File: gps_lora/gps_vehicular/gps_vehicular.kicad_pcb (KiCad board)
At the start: 2 copper layers, 71.1 x 41.3 mm, 53 parts, among them J1 IN 12V, J2 USB_B, J3 ADJ, J4 BAT, J5 IGN, J6 RELAY, J7 PANI, J8 SWD, Q1 Q_PMOS_GSD, Q2 SMMBT3904LT1G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

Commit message: add pcb gps vehicular and minimo
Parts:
- AE1, D9, Q3, R10, R11, R12, R13, R14, R15, U4, U5, U7: moved to F.Cu
- C7, D5, D6, D7, J1, J2, J3, J4, J5, J6, J7, J8, MODULE1, R3, R6, R8, SW1: moved to B.Cu
- moved D5 25.6 mm to (118.4, 55.9)
- moved R11 24.8 mm to (133.9, 78.7)
- moved U7 23.7 mm to (163.3, 82.5), turned to 180 degrees
- moved D9 23.3 mm to (163.8, 86.9)
- moved R3 22.6 mm to (118.4, 61.7)
- moved R15 21.3 mm to (162.1, 79.0)
- moved R13 19.7 mm to (143.0, 82.3), turned to 90 degrees
- moved R14 18.8 mm to (169.4, 82.3), turned to 90 degrees
- moved U4 18.6 mm to (135.1, 82.5), turned to 180 degrees
- moved R10 18.4 mm to (140.2, 87.4)
- moved D7 15.9 mm to (123.2, 56.0), turned to 90 degrees
- moved C5 15.3 mm to (114.8, 82.3), turned to 180 degrees
- moved R9 15.2 mm to (123.7, 82.0), turned to 90 degrees
- moved Q3 14.9 mm to (151.6, 86.7), turned to 0 degrees
- moved C1 14.5 mm to (114.8, 66.8), turned to 180 degrees
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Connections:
- U6 pad 1: Net-(U6-Pad1) -> /microcontroller/LED_1
- U6 pad 12: Net-(U6-Pad12) -> /microcontroller/SIG_PANI
- U6 pad 15: Net-(U6-Pad15) -> /microcontroller/1PPS
- U6 pad 2: Net-(U6-Pad2) -> /microcontroller/LED_2
- U6 pad 6: Net-(U6-Pad6) -> /microcontroller/SIG_CONECTADO
- U6 pad 7: Net-(U6-Pad7) -> /microcontroller/SIG_IGNI
- U6 pad 8: Net-(U6-Pad8) -> /microcontroller/OUT_SIG
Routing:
- net +3V3: track 0.00 -> 200.1 mm, vias 0 -> 4
- net +5V: track 0.00 -> 63.7 mm, vias 0 -> 2
- net +12V: track 0.00 -> 58.5 mm
- net D+: track 0.00 -> 37.8 mm, vias 0 -> 1
- net D-: track 0.00 -> 37.8 mm, vias 0 -> 1
- net +BATT: track 0.00 -> 37.8 mm
- net Net-(R3-Pad2): track 0.00 -> 36.7 mm, vias 0 -> 3
- net /microcontroller/SIG_PANI: track 0.00 -> 35.6 mm
- net /microcontroller/SIG_CONECTADO: track 0.00 -> 30.8 mm, vias 0 -> 1
- net /microcontroller/DIO0: track 0.00 -> 29.3 mm, vias 0 -> 2
- net GND: track 0.00 -> 27.8 mm, vias 0 -> 9
- net /microcontroller/DIO1: track 0.00 -> 24.6 mm, vias 0 -> 2
- net /microcontroller/DIO2: track 0.00 -> 22.7 mm
- net /microcontroller/RX_GPS: track 0.00 -> 22.5 mm, vias 0 -> 1
- net /microcontroller/LED_2: track 0.00 -> 21.2 mm, vias 0 -> 1
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- added copper zone on B.Cu, net GND
- added copper zone on F.Cu, net GND
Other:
- board size 71.1 x 41.3 mm -> 71.1 x 42.8 mm
- net class Default: trace_width 0.25 -> 0.3; via_drill 0.4 -> 0.3
- net class Source added: clearance 0.2, trace_width 0.5, via_dia 0.9, via_drill 0.45
- board text added: "+"
- board text added: "-"
- board text added: "1"

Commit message: add logos
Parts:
- added G***: LOGO, Aesthetics:electronic_cats_logo_8x6, B.Cu at (158.6, 56.8)
- added REF***: OSHW-Logo_7.5x8mm_SilkScreen, Symbols:OSHW-Logo_7.5x8mm_SilkScreen, F.Cu at (122.8, 56.1)
- added REF***: FCC-Logo_7.3x6mm_SilkScreen, Symbols:FCC-Logo_7.3x6mm_SilkScreen, F.Cu at (108.1, 86.4)

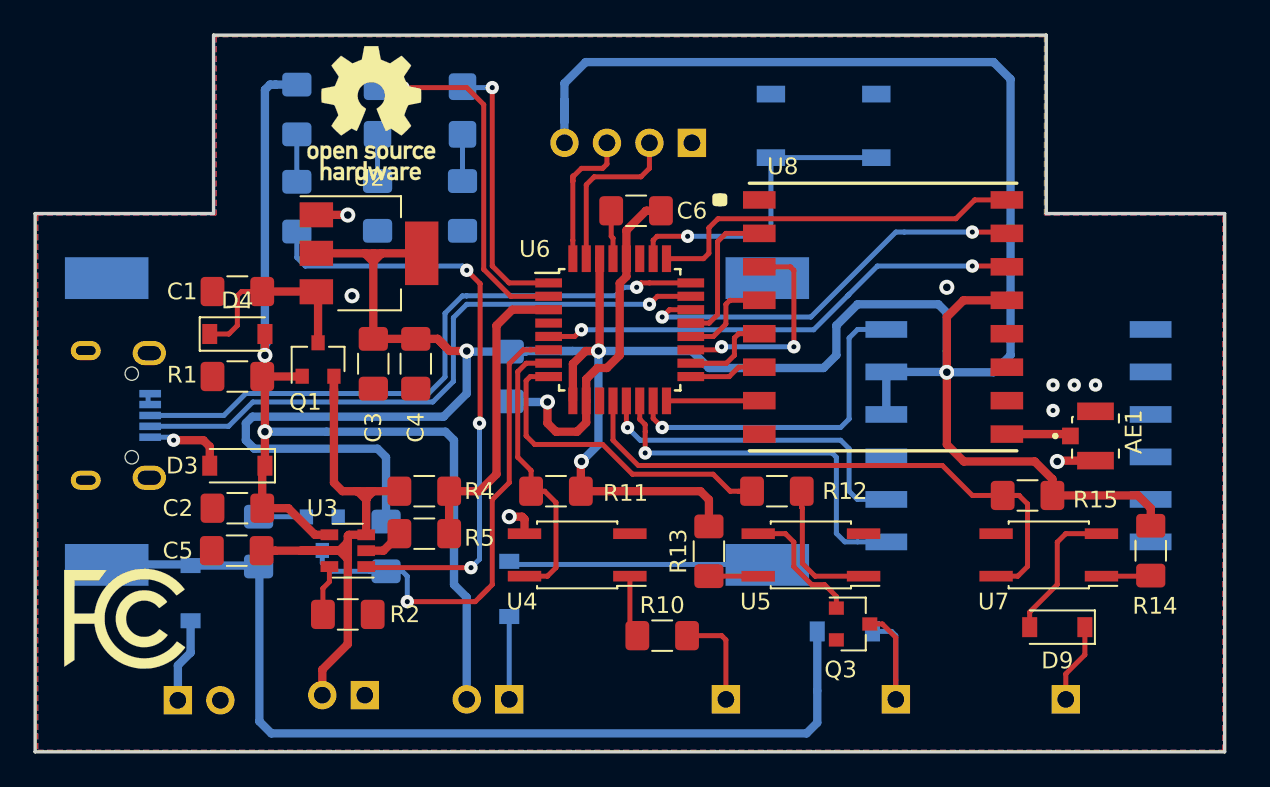
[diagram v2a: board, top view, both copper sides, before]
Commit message: Round off the corners and change screen printing gps_vehicular
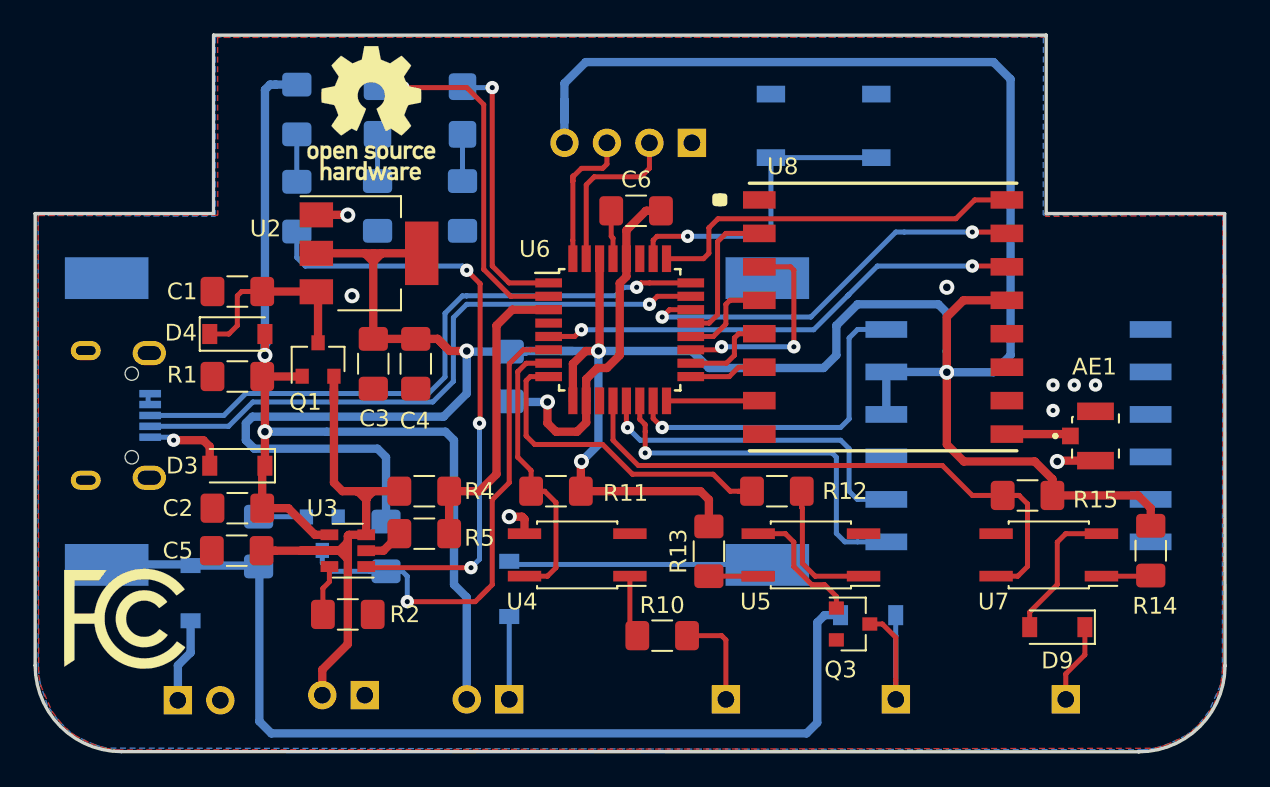
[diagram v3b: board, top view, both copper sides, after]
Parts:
- moved D8 1.70 mm to (152.5, 86.2)
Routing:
- net +12V: track 58.5 -> 60.6 mm
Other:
- outline, holes or cut-outs redrawn
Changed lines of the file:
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@@
-(kicad_pcb (version 20171130) (host pcbnew "(5.0.1-3-g963ef8bb5)")
+(kicad_pcb (version 20171130) (host pcbnew "(5.1.0)-1")
   (general
     (thickness 1.6)
-    (drawings 14)
-    (tracks 470)
+    (drawings 16)
+    (tracks 471)
     (zones 0)
     (modules 56)
@@
     (zone_45_only no)
     (trace_min 0.2)
-    (segment_width 0.2)
-    (edge_width 0.15)
     (via_size 0.8)
     (via_drill 0.3)
@@
     (uvia_min_size 0.2)
     (uvia_min_drill 0.1)
+    (edge_width 0.15)
+    (segment_width 0.2)
     (pcb_text_width 0.3)
     (pcb_text_size 1.5 1.5)
@@
     (at 166.116 75.438 270)
     (attr smd)
-    (fp_text reference AE1 (at -0.254 -2.286 90) (layer F.SilkS)
+    (fp_text reference AE1 (at -4.138 0.066 180) (layer F.SilkS)
       (effects (font (size 1 1) (thickness 0.15)))
     )
@@
     (tags "capacitor handsolder")
     (attr smd)
-    (fp_text reference C3 (at 3.81 0 270) (layer F.SilkS)
+    (fp_text reference C3 (at 3.27 -0.064) (layer F.SilkS)
       (effects (font (size 1 1) (thickness 0.15)))
     )
@@
     (tags "capacitor handsolder")
     (attr smd)
-    (fp_text reference C4 (at 3.81 0 270) (layer F.SilkS)
+    (fp_text reference C4 (at 3.41 0.046) (layer F.SilkS)
       (effects (font (size 1 1) (thickness 0.15)))
     )
@@
     (tags "capacitor handsolder")
     (attr smd)
-    (fp_text reference C6 (at 3.3385 0) (layer F.SilkS)
+    (fp_text reference C6 (at 0.0125 -1.866) (layer F.SilkS)
       (effects (font (size 1 1) (thickness 0.15)))
     )
@@
     (tags "capacitor handsolder")
     (attr smd)
-    (fp_text reference C7 (at 0 1.82 270) (layer B.SilkS)
+    (fp_text reference C7 (at -3.252 -0.106) (layer B.SilkS)
       (effects (font (size 1 1) (thickness 0.15)) (justify mirror))
     )
@@
     (tags SOD-123)
     (attr smd)
-    (fp_text reference D1 (at -3.302 0 90) (layer B.SilkS)
+    (fp_text reference D1 (at -3.302 0 180) (layer B.SilkS)
       (effects (font (size 1 1) (thickness 0.15)) (justify mirror))
     )
@@
     (tags SOD-123)
     (attr smd)
-    (fp_text reference D2 (at 3.556 0 90) (layer B.SilkS)
+    (fp_text reference D2 (at 3.556 0 180) (layer B.SilkS)
       (effects (font (size 1 1) (thickness 0.15)) (justify mirror))
     )
@@
   )
   (module Diode_SMD:D_SOD-123 (layer B.Cu)
-    (at 151.13 87.122)
+    (at 152.52 86.15)
     (descr SOD-123)
     (tags SOD-123)
@@
       (effects (font (size 1 1) (thickness 0.05)))
     )
-    (fp_text value L80-M39 (at 5.3 -7.55 180) (layer B.SilkS)
+    (fp_text value L80-M39 (at -5.12 9.04 180) (layer B.SilkS)
       (effects (font (size 1 1) (thickness 0.15)) (justify mirror))
     )
@@
     (tags SOT-23)
     (attr smd)
-    (fp_text reference Q2 (at 2.794 0 90) (layer B.SilkS)
+    (fp_text reference Q2 (at -2.58 -0.052 180) (layer B.SilkS)
       (effects (font (size 1 1) (thickness 0.15)) (justify mirror))
     )
@@
     (tags "resistor handsolder")
     (attr smd)
-    (fp_text reference R7 (at 3.5925 0 90) (layer B.SilkS)
+    (fp_text reference R7 (at -3.4215 0.028 180) (layer B.SilkS)
       (effects (font (size 1 1) (thickness 0.15)) (justify mirror))
     )
@@
     (tags "resistor handsolder")
     (attr smd)
-    (fp_text reference R9 (at -3.556 0 90) (layer B.SilkS)
+    (fp_text reference R9 (at 3.212 0.012 180) (layer B.SilkS)
       (effects (font (size 1 1) (thickness 0.15)) (justify mirror))
     )
@@
     (tags "CMS SOT")
     (attr smd)
-    (fp_text reference U2 (at 0 -4.5) (layer F.SilkS)
+    (fp_text reference U2 (at -6.192 -1.476) (layer F.SilkS)
       (effects (font (size 1 1) (thickness 0.15)))
     )
@@
   (module gps_LoRa:LM2596DC-DC (layer B.Cu)
     (at 105.156 85.09)
-    (fp_text reference U1 (at 4.365 -0.9135) (layer B.SilkS)
+    (fp_text reference U1 (at 2.054 0.9) (layer B.SilkS)
       (effects (font (size 1 1) (thickness 0.15)) (justify mirror))
     )
@@
     (tags SOD-123)
     (attr smd)
-    (fp_text reference D4 (at 0 -2) (layer F.SilkS)
+    (fp_text reference D4 (at -3.378 -0.072) (layer F.SilkS)
       (effects (font (size 1 1) (thickness 0.15)))
     )
@@
       (xy 1.372452 -1.683595)) (layer F.SilkS) (width 0.01))
   )
+  (gr_arc (start 168.71 89.17) (end 168.71 94.32) (angle -90) (layer Edge.Cuts) (width 0.2))
+  (gr_arc (start 107.87 89.16) (end 102.72 89.16) (angle -90) (layer Edge.Cuts) (width 0.2))
   (dimension 16.256 (width 0.15) (layer Margin)
     (gr_text "16.256 mm" (at 100.046 86.106 90) (layer Margin)
@@
   )
   (gr_line (start 113.386 51.472) (end 113.386 62.14) (layer Edge.Cuts) (width 0.2))
-  (gr_line (start 102.718 62.14) (end 102.718 94.3218) (layer Edge.Cuts) (width 0.2))
-  (gr_line (start 173.838 94.3218) (end 173.838 62.14) (layer Edge.Cuts) (width 0.2))
+  (gr_line (start 102.718 62.14) (end 102.72 89.16) (layer Edge.Cuts) (width 0.2))
+  (gr_line (start 173.86 89.17) (end 173.838 62.14) (layer Edge.Cuts) (width 0.2))
   (gr_line (start 173.838 62.14) (end 163.17 62.14) (layer Edge.Cuts) (width 0.2))
   (gr_line (start 163.17 51.472) (end 113.386 51.472) (layer Edge.Cuts) (width 0.2))
-  (gr_line (start 102.718 94.3218) (end 173.838 94.3218) (layer Edge.Cuts) (width 0.2))
+  (gr_line (start 107.87 94.31) (end 168.71 94.32) (layer Edge.Cuts) (width 0.2))
   (gr_line (start 113.386 62.14) (end 102.718 62.14) (layer Edge.Cuts) (width 0.2))
   (gr_line (start 163.17 62.14) (end 163.17 51.472) (layer Edge.Cuts) (width 0.2))
@@
   (segment (start 116.025 83.186) (end 116.078 83.239) (width 0.5) (layer B.Cu) (net 8))
   (segment (start 112.014 83.186) (end 116.025 83.186) (width 0.5) (layer B.Cu) (net 8))
-  (segment (start 116.078 83.239) (end 116.12379 83.28479) (width 0.5) (layer B.Cu) (net 8))
-  (segment (start 149.48 90.678) (end 149.48 87.122) (width 0.5) (layer B.Cu) (net 8))
-  (segment (start 116.12379 83.28479) (end 116.12379 92.50179) (width 0.5) (layer B.Cu) (net 8))
-  (segment (start 116.12379 92.50179) (end 116.84 93.218) (width 0.5) (layer B.Cu) (net 8))
-  (segment (start 116.84 93.218) (end 148.844 93.218) (width 0.5) (layer B.Cu) (net 8))
-  (segment (start 148.844 93.218) (end 149.48 92.582) (width 0.5) (layer B.Cu) (net 8))
-  (segment (start 149.48 92.582) (end 149.48 90.678) (width 0.5) (layer B.Cu) (net 8))
+  (segment (start 116.12379 83.28479) (end 116.078 83.239) (width 0.5) (layer B.Cu) (net 8))
+  (segment (start 116.12379 92.50179) (end 116.12379 83.28479) (width 0.5) (layer B.Cu) (net 8))
+  (segment (start 150.87 86.15) (end 149.92 86.15) (width 0.5) (layer B.Cu) (net 8))
+  (segment (start 149.92 86.15) (end 149.48 86.59) (width 0.5) (layer B.Cu) (net 8))
+  (segment (start 149.48 86.59) (end 149.48 92.582) (width 0.5) (layer B.Cu) (net 8))
+  (segment (start 149.48 92.582) (end 148.844 93.218) (width 0.5) (layer B.Cu) (net 8))
+  (segment (start 148.844 93.218) (end 116.84 93.218) (width 0.5) (layer B.Cu) (net 8))
+  (segment (start 116.84 93.218) (end 116.12379 92.50179) (width 0.5) (layer B.Cu) (net 8))
   (segment (start 131.064 86.232) (end 131.064 91.186) (width 0.3) (layer B.Cu) (net 9))
   (segment (start 131.252 83.12) (end 131.064 82.932) (width 0.3) (layer B.Cu) (net 10))
@@
   (segment (start 153.372 86.68) (end 154.178 87.486) (width 0.3) (layer F.Cu) (net 17))
   (segment (start 152.622 86.68) (end 153.372 86.68) (width 0.3) (layer F.Cu) (net 17))
-  (segment (start 153.924 87.122) (end 152.78 87.122) (width 0.3) (layer B.Cu) (net 17))
   (segment (start 154.178 91.186) (end 154.178 87.376) (width 0.3) (layer B.Cu) (net 17))
-  (segment (start 154.178 87.376) (end 153.924 87.122) (width 0.3) (layer B.Cu) (net 17))
+  (segment (start 154.17 87.368) (end 154.17 86.15) (width 0.3) (layer B.Cu) (net 17))
+  (segment (start 154.178 87.376) (end 154.17 87.368) (width 0.3) (layer B.Cu) (net 17))
   (segment (start 164.338 91.186) (end 164.338 89.662) (width 0.3) (layer F.Cu) (net 18))
   (segment (start 165.48 88.52) (end 165.48 86.868) (width 0.3) (layer F.Cu) (net 18))
@@
     (connect_pads (clearance 0.508))
     (min_thickness 0.254)
-    (fill yes (arc_segments 16) (thermal_gap 0.508) (thermal_bridge_width 0.508))
+    (fill yes (arc_segments 32) (thermal_gap 0.508) (thermal_bridge_width 0.508))
     (polygon
       (pts
-        (xy 113.538 51.562) (xy 113.538 62.23) (xy 102.87 62.23) (xy 102.87 94.234) (xy 173.736 94.234)
-        (xy 173.736 62.23) (xy 163.068 62.23) (xy 163.068 51.562)
+        (xy 173.73 62.25) (xy 173.7 89.71) (xy 173.6 90.3) (xy 172.9 91.9) (xy 172.2 92.8)
+        (xy 171.55 93.33) (xy 170.58 93.81) (xy 169.7 94.1) (xy 169.24 94.17) (xy 168.99 94.2)
+        (xy 107 94.1) (xy 106.6 94) (xy 106.3 93.91) (xy 105.2 93.41) (xy 104.85 93.18)
+        (xy 104.11 92.46) (xy 103.46 91.57) (xy 103.02 90.24) (xy 102.9 89.3) (xy 102.9 62.25)
+        (xy 113.5 62.3) (xy 113.5 51.58) (xy 163 51.6) (xy 162.99 62.23)
       )
     )
@@
     (connect_pads (clearance 0.508))
     (min_thickness 0.254)
-    (fill yes (arc_segments 16) (thermal_gap 0.508) (thermal_bridge_width 0.508))
+    (fill yes (arc_segments 32) (thermal_gap 0.508) (thermal_bridge_width 0.508))
     (polygon
       (pts
-        (xy 113.538 51.562) (xy 113.538 62.23) (xy 102.87 62.23) (xy 102.87 94.234) (xy 173.736 94.234)
-        (xy 173.736 62.23) (xy 163.068 62.23) (xy 163.068 51.562)
+        (xy 102.9 62.26) (xy 102.93 89.72) (xy 103.03 90.31) (xy 103.73 91.91) (xy 104.43 92.81)
+        (xy 105.08 93.34) (xy 106.05 93.82) (xy 106.93 94.11) (xy 107.39 94.18) (xy 107.64 94.21)
+        (xy 169.63 94.11) (xy 170.03 94.01) (xy 170.33 93.92) (xy 171.43 93.42) (xy 171.78 93.19)
+        (xy 172.52 92.47) (xy 173.17 91.58) (xy 173.61 90.25) (xy 173.73 89.31) (xy 173.73 62.26)
+        (xy 163.13 62.31) (xy 163.13 51.59) (xy 113.63 51.61) (xy 113.64 62.24)
       )
     )

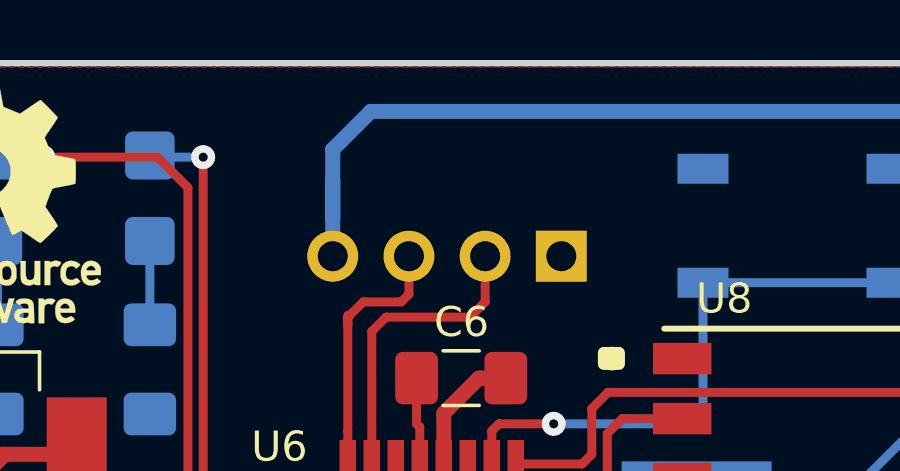
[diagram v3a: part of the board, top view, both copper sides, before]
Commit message: add screen printing swd pins gps_vehicular
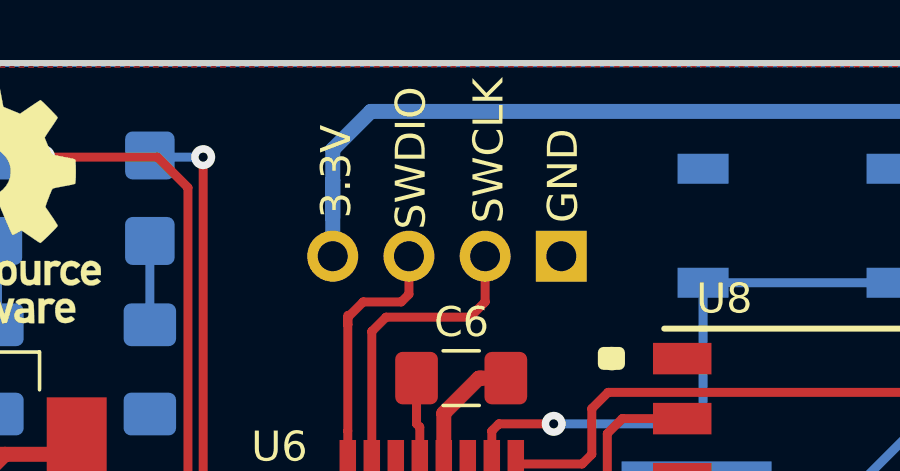
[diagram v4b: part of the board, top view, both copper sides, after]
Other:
- board text added: "3.3V"
- board text added: "GND"
- board text added: "SWCLK"
- board text added: "SWDIO"
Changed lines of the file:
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@@
   (general
     (thickness 1.6)
-    (drawings 16)
+    (drawings 20)
     (tracks 471)
     (zones 0)
@@
       (xy 1.372452 -1.683595)) (layer F.SilkS) (width 0.01))
   )
+  (gr_text "GND\n" (at 142.04 55.23 90) (layer F.SilkS)
+    (effects (font (size 1 1) (thickness 0.15)))
+  )
+  (gr_text SWCLK (at 139.56 54.39 90) (layer F.SilkS)
+    (effects (font (size 1 1) (thickness 0.15)))
+  )
+  (gr_text "SWDIO\n" (at 136.97 54.64 90) (layer F.SilkS)
+    (effects (font (size 1 1) (thickness 0.15)))
+  )
+  (gr_text 3.3V (at 134.48 55.09 90) (layer F.SilkS)
+    (effects (font (size 1 1) (thickness 0.15)))
+  )
   (gr_arc (start 168.71 89.17) (end 168.71 94.32) (angle -90) (layer Edge.Cuts) (width 0.2))
